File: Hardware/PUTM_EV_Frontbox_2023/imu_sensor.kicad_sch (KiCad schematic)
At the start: 3 parts, among them J2 Conn_01x05, J3 Conn_01x05, U17 IMS330DHCX

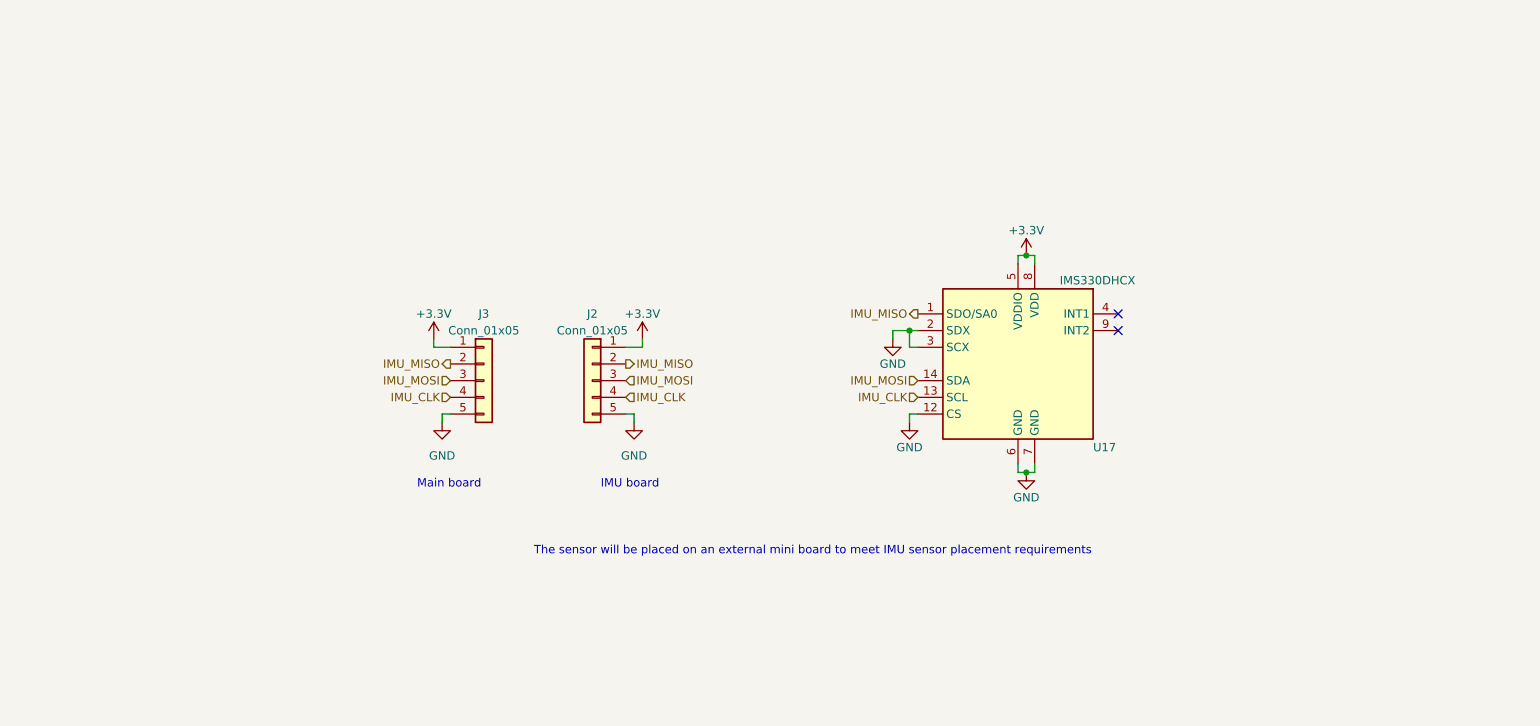
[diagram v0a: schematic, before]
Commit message: Added power section, replaced SWPS
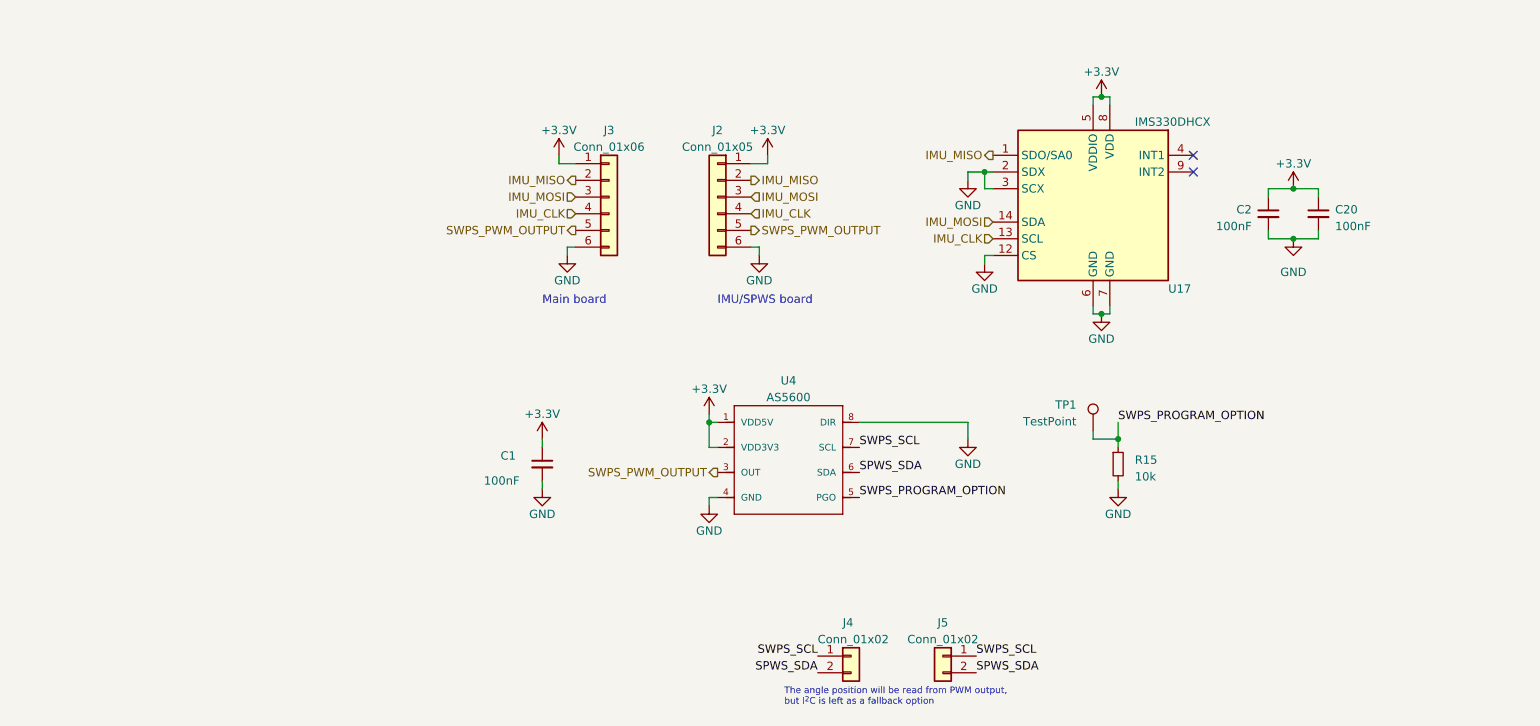
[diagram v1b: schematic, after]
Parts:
- added C1, C2, C20: 100nF, symbol Device:C_Small
- added J4, J5: Conn_01x02, symbol Connector_Generic:Conn_01x02
- added R15: 10k, symbol Device:R_Small
- added TP1: TestPoint, symbol Connector:TestPoint
- added U4: AS5600, AS5600, symbol AS5600:AS5600
- J2: symbol Connector_Generic:Conn_01x05 -> Connector_Generic:Conn_01x06
- J3: value Conn_01x05 -> Conn_01x06; symbol Connector_Generic:Conn_01x05 -> Connector_Generic:Conn_01x06
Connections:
- net +3.3V: now also C1.1, C2.1, C20.1, U4.1 (VDD5V), U4.2 (VDD3V3)
- net GND: now also J2.6 (Pin_6), J3.6 (Pin_6), C1.2, C2.2, C20.2, R15.2, U4.4 (GND), U4.8 (DIR); no longer J2.5 (Pin_5), J3.5 (Pin_5)
- new net SPWS_SDA: J4.2 (Pin_2), J5.2 (Pin_2), U4.6 (SDA)
- new net SWPS_PROGRAM_OPTION: R15.1, TP1.1, U4.5 (PGO)
- new net SWPS_PWM_OUTPUT: J2.5 (Pin_5), J3.5 (Pin_5), U4.3 (OUT)
- new net SWPS_SCL: J4.1 (Pin_1), J5.1 (Pin_1), U4.7 (SCL)
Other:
- note added: "IMU/SPWS board"
- note added: "The angle position will be read from PWM output, but I^{2}C is left as a fallback option"
- note removed: "IMU board"
- note removed: "The sensor will be placed on an external mini board to meet IMU sensor placement requirements"
- title: ISM330DHCX Sensor -> ISM330DHCX Sensor/Steering wheel position sensor
- moved on the sheet: U17

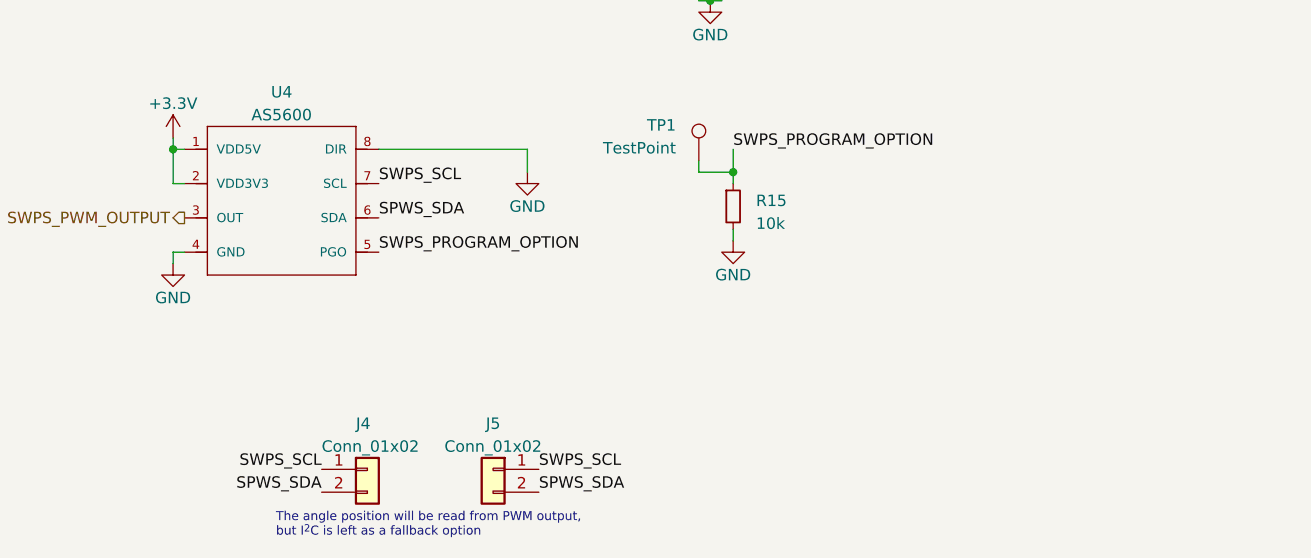
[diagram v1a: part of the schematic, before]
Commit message: Added MCU wiring
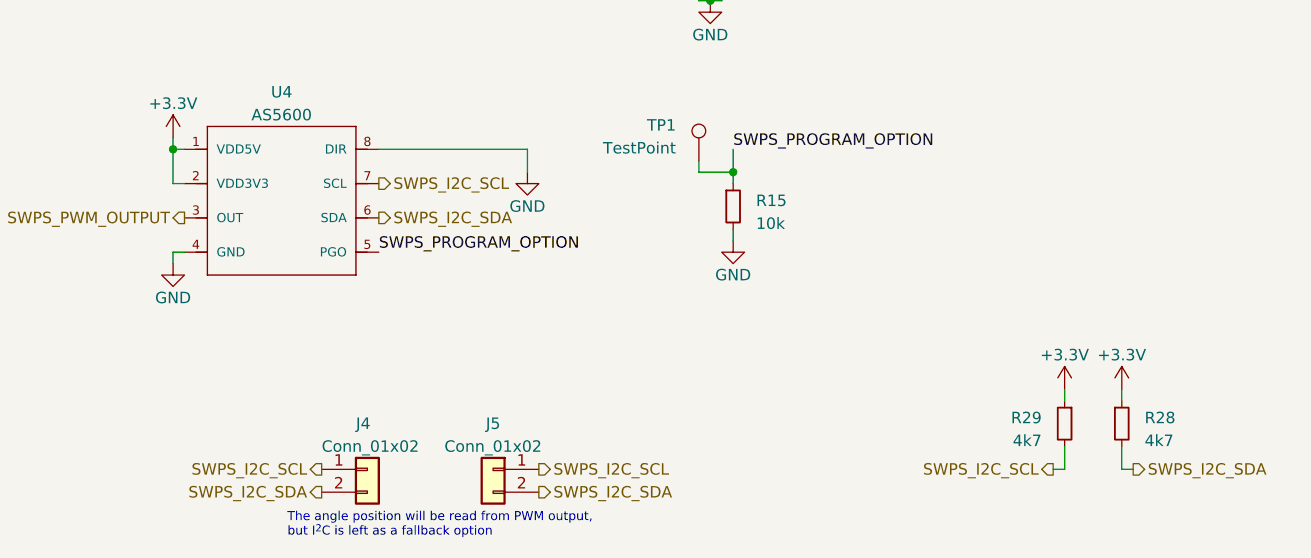
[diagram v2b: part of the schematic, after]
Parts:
- added R28, R29: 4k7, symbol Device:R_Small
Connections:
- net +3.3V: now also R28.1, R29.1
- net SPWS_SDA renamed SWPS_I2C_SDA
- net SWPS_I2C_SDA: now also R28.2
- net SWPS_SCL renamed SWPS_I2C_SCL
- net SWPS_I2C_SCL: now also R29.2
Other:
- title: ISM330DHCX Sensor/Steering wheel position sensor -> IMU and SWPS sensor
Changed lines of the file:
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@@
   (paper "A4")
   (title_block
-    (title "ISM330DHCX Sensor/Steering wheel position sensor")
+    (title "IMU and SWPS sensor")
     (date "2023-02-24")
     (rev "${REVISION}")
@@
     (stroke (width 0) (type default))
   )
+  (wire (pts (xy 228.6 147.32) (xy 228.6 144.78))
+    (stroke (width 0) (type default))
+  )
   (wire (pts (xy 129.54 72.39) (xy 132.08 72.39))
     (stroke (width 0) (type default))
   )
+  (wire (pts (xy 228.6 138.43) (xy 228.6 139.7))
+    (stroke (width 0) (type default))
+  )
   (wire (pts (xy 166.37 73.66) (xy 165.1 73.66))
     (stroke (width 0) (type default))
@@
     (stroke (width 0) (type default))
   )
+  (wire (pts (xy 222.25 138.43) (xy 222.25 139.7))
+    (stroke (width 0) (type default))
+  )
   (wire (pts (xy 181.61 95.25) (xy 182.88 95.25))
     (stroke (width 0) (type default))
@@
     (stroke (width 0) (type default))
   )
+  (wire (pts (xy 229.87 147.32) (xy 228.6 147.32))
+    (stroke (width 0) (type default))
+  )
   (wire (pts (xy 181.61 113.03) (xy 181.61 114.3))
     (stroke (width 0) (type default))
   )
+  (wire (pts (xy 220.98 147.32) (xy 222.25 147.32))
+    (stroke (width 0) (type default))
+  )
   (wire (pts (xy 165.1 86.36) (xy 166.37 86.36))
     (stroke (width 0) (type default))
@@
     (stroke (width 0) (type default))
   )
+  (wire (pts (xy 222.25 147.32) (xy 222.25 144.78))
+    (stroke (width 0) (type default))
+  )
   (wire (pts (xy 208.28 83.82) (xy 212.09 83.82))
     (stroke (width 0) (type default))
@@
   )
   (text "The angle position will be read from PWM output,\nbut I^{2}C is left as a fallback option"
-    (at 134.62 154.94 0)
+    (at 135.89 154.94 0)
     (effects (font (size 1 1)) (justify left bottom))
   )
@@
     (effects (font (size 1.27 1.27)) (justify left bottom))
   )
-  (label "SPWS_SDA" (at 139.7 149.86 180) (fields_autoplaced)
-    (effects (font (size 1.27 1.27)) (justify right bottom))
-  )
-  (label "SWPS_SCL" (at 163.83 147.32 0) (fields_autoplaced)
-    (effects (font (size 1.27 1.27)) (justify left bottom))
-  )
-  (label "SWPS_SCL" (at 139.7 147.32 180) (fields_autoplaced)
-    (effects (font (size 1.27 1.27)) (justify right bottom))
-  )
   (label "SWPS_PROGRAM_OPTION" (at 185.42 111.76 0) (fields_autoplaced)
     (effects (font (size 1.27 1.27)) (justify left bottom))
   )
-  (label "SPWS_SDA" (at 163.83 149.86 0) (fields_autoplaced)
-    (effects (font (size 1.27 1.27)) (justify left bottom))
-  )
-  (label "SPWS_SDA" (at 146.05 119.38 0) (fields_autoplaced)
-    (effects (font (size 1.27 1.27)) (justify left bottom))
-  )
   (label "SWPS_PROGRAM_OPTION" (at 146.05 123.19 0) (fields_autoplaced)
     (effects (font (size 1.27 1.27)) (justify left bottom))
   )
-  (label "SWPS_SCL" (at 146.05 115.57 0) (fields_autoplaced)
-    (effects (font (size 1.27 1.27)) (justify left bottom))
-  )
   (hierarchical_label "IMU_MOSI" (shape input) (at 129.54 77.47 0) (fields_autoplaced)
     (effects (font (size 1.27 1.27)) (justify left))
@@
     (effects (font (size 1.27 1.27)) (justify right))
   )
+  (hierarchical_label "SWPS_I2C_SDA" (shape output) (at 163.83 149.86 0) (fields_autoplaced)
+    (effects (font (size 1.27 1.27)) (justify left))
+  )
   (hierarchical_label "IMU_CLK" (shape input) (at 102.87 80.01 180) (fields_autoplaced)
     (effects (font (size 1.27 1.27)) (justify right))
@@
     (effects (font (size 1.27 1.27)) (justify right))
   )
+  (hierarchical_label "SWPS_I2C_SCL" (shape output) (at 146.05 115.57 0) (fields_autoplaced)
+    (effects (font (size 1.27 1.27)) (justify left))
+  )
+  (hierarchical_label "SWPS_I2C_SDA" (shape output) (at 146.05 119.38 0) (fields_autoplaced)
+    (effects (font (size 1.27 1.27)) (justify left))
+  )
+  (hierarchical_label "SWPS_I2C_SDA" (shape output) (at 139.7 149.86 180) (fields_autoplaced)
+    (effects (font (size 1.27 1.27)) (justify right))
+  )
   (hierarchical_label "SWPS_PWM_OUTPUT" (shape output) (at 102.87 82.55 180) (fields_autoplaced)
     (effects (font (size 1.27 1.27)) (justify right))
+  )
+  (hierarchical_label "SWPS_I2C_SCL" (shape output) (at 163.83 147.32 0) (fields_autoplaced)
+    (effects (font (size 1.27 1.27)) (justify left))
   )
   (hierarchical_label "SWPS_PWM_OUTPUT" (shape output) (at 129.54 82.55 0) (fields_autoplaced)
     (effects (font (size 1.27 1.27)) (justify left))
   )
+  (hierarchical_label "SWPS_I2C_SCL" (shape output) (at 220.98 147.32 180) (fields_autoplaced)
+    (effects (font (size 1.27 1.27)) (justify right))
+  )
   (hierarchical_label "IMU_MISO" (shape output) (at 129.54 74.93 0) (fields_autoplaced)
     (effects (font (size 1.27 1.27)) (justify left))
   )
+  (hierarchical_label "SWPS_I2C_SCL" (shape output) (at 139.7 147.32 180) (fields_autoplaced)
+    (effects (font (size 1.27 1.27)) (justify right))
+  )
   (hierarchical_label "IMU_MOSI" (shape input) (at 166.37 81.28 180) (fields_autoplaced)
     (effects (font (size 1.27 1.27)) (justify right))
   )
   (hierarchical_label "IMU_CLK" (shape input) (at 129.54 80.01 0) (fields_autoplaced)
+    (effects (font (size 1.27 1.27)) (justify left))
+  )
+  (hierarchical_label "SWPS_I2C_SDA" (shape output) (at 229.87 147.32 0) (fields_autoplaced)
     (effects (font (size 1.27 1.27)) (justify left))
   )
@@
         (path "/b652b05a-4e3d-4ad1-b032-18886abe7d45/fc1ffdcd-7b51-43f2-87c4-9a5d8609cd78"
           (reference "J3") (unit 1)
+        )
+      )
+    )
+  )
+  (symbol (lib_id "power:+3.3V") (at 228.6 138.43 0) (unit 1)
+    (in_bom yes) (on_board yes) (dnp no) (fields_autoplaced)
+    (property "Reference" "#PWR090" (at 228.6 142.24 0)
+      (effects (font (size 1.27 1.27)) hide)
+    )
+    (property "Value" "+3.3V" (at 228.6 134.62 0)
+      (effects (font (size 1.27 1.27)))
+    )
+    (property "Footprint" "" (at 228.6 138.43 0)
+      (effects (font (size 1.27 1.27)) hide)
+    )
+    (property "Datasheet" "" (at 228.6 138.43 0)
+      (effects (font (size 1.27 1.27)) hide)
+    )
+    (pin "1")
+    (instances
+      (project "PUTM_EV_Frontbox_2023"
+        (path "/b652b05a-4e3d-4ad1-b032-18886abe7d45/fc1ffdcd-7b51-43f2-87c4-9a5d8609cd78"
+          (reference "#PWR090") (unit 1)
         )
       )
@@
     )
   )
+  (symbol (lib_id "power:+3.3V") (at 222.25 138.43 0) (unit 1)
+    (in_bom yes) (on_board yes) (dnp no) (fields_autoplaced)
+    (property "Reference" "#PWR089" (at 222.25 142.24 0)
+      (effects (font (size 1.27 1.27)) hide)
+    )
+    (property "Value" "+3.3V" (at 222.25 134.62 0)
+      (effects (font (size 1.27 1.27)))
+    )
+    (property "Footprint" "" (at 222.25 138.43 0)
+      (effects (font (size 1.27 1.27)) hide)
+    )
+    (property "Datasheet" "" (at 222.25 138.43 0)
+      (effects (font (size 1.27 1.27)) hide)
+    )
+    (pin "1")
+    (instances
+      (project "PUTM_EV_Frontbox_2023"
+        (path "/b652b05a-4e3d-4ad1-b032-18886abe7d45/fc1ffdcd-7b51-43f2-87c4-9a5d8609cd78"
+          (reference "#PWR089") (unit 1)
+        )
+      )
+    )
+  )
   (symbol (lib_id "power:GND") (at 212.09 83.82 0) (unit 1)
     (in_bom yes) (on_board yes) (dnp no) (fields_autoplaced)
@@
         (path "/b652b05a-4e3d-4ad1-b032-18886abe7d45/fc1ffdcd-7b51-43f2-87c4-9a5d8609cd78"
           (reference "#PWR016") (unit 1)
+        )
+      )
+    )
+  )
+  (symbol (lib_id "Device:R_Small") (at 222.25 142.24 0) (mirror y) (unit 1)
+    (in_bom yes) (on_board yes) (dnp no)
+    (property "Reference" "R29" (at 219.71 141.605 0)
+      (effects (font (size 1.27 1.27)) (justify left))
+    )
+    (property "Value" "4k7" (at 219.71 144.145 0)
+      (effects (font (size 1.27 1.27)) (justify left))
+    )
+    (property "Footprint" "" (at 222.25 142.24 0)
+      (effects (font (size 1.27 1.27)) hide)
+    )
+    (property "Datasheet" "~" (at 222.25 142.24 0)
+      (effects (font (size 1.27 1.27)) hide)
+    )
+    (pin "1")
+    (pin "2")
+    (instances
+      (project "PUTM_EV_Frontbox_2023"
+        (path "/b652b05a-4e3d-4ad1-b032-18886abe7d45/fc1ffdcd-7b51-43f2-87c4-9a5d8609cd78"
+          (reference "R29") (unit 1)
         )
       )
@@
         )
       )
+    )
+  )
+  (symbol (lib_id "Device:R_Small") (at 228.6 142.24 0) (unit 1)
+    (in_bom yes) (on_board yes) (dnp no) (fields_autoplaced)
+    (property "Reference" "R28" (at 231.14 141.605 0)
+      (effects (font (size 1.27 1.27)) (justify left))
+    )
+    (property "Value" "4k7" (at 231.14 144.145 0)
+      (effects (font (size 1.27 1.27)) (justify left))
+    )
+    (property "Footprint" "" (at 228.6 142.24 0)
+      (effects (font (size 1.27 1.27)) hide)
+    )
+    (property "Datasheet" "~" (at 228.6 142.24 0)
+      (effects (font (size 1.27 1.27)) hide)
+    )
+    (pin "1")
+    (pin "2")
+    (instances
+      (project "PUTM_EV_Frontbox_2023"
+        (path "/b652b05a-4e3d-4ad1-b032-18886abe7d45/fc1ffdcd-7b51-43f2-87c4-9a5d8609cd78"
+          (reference "R28") (unit 1)
+        )
+      )

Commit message: Schematic ready for review
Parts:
- U17: symbol karta_pomiarowa_v2-rescue:LSM6DS3-Sensor_Motionn -> ISM330DHCX:LSM6DS3
- renumbered C1 to C2, C2 to C3, C20 to C4, J3 to J5, J2 to J6, J4 to J7, J5 to J8, R15 to R6, R29 to R7, R28 to R8, U4 to U2

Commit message: Fixed all issues
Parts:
- added C42: 1nF, symbol Device:C_Small
- added FB6, FB7: 60R@100MHz, symbol Device:FerriteBead_Small
- added R78: 1k, symbol Device:R_Small
- added TP10, TP7, TP8, TP9: TestPoint, symbol Connector:TestPoint
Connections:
- net +3.3V: now also FB6.1, FB7.1; no longer U17.5 (VDDIO), U17.8 (VDD), U2.1 (VDD5V), U2.2 (VDD3V3)
- net GND: now also C42.2
- net IMU_CLK: now also TP9.1
- net IMU_MISO: now also TP7.1
- net IMU_MOSI: now also TP8.1
- net SWPS_PWM_OUTPUT: now also C42.1, R78.2; no longer U2.3 (OUT)
- new net: FB7.2, U2.1 (VDD5V), U2.2 (VDD3V3)
- new net: FB6.2, U17.5 (VDDIO), U17.8 (VDD)
- new net SWPS_RAW_PWM_OUTPUT: R78.1, TP10.1, U2.3 (OUT)
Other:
- note added: "IC is used in mode 1 >>>"
- note added: "IMU/SWPS board"
- note added: "The min unfiltered rise time is 1.8 us"
- note removed: "IMU/SPWS board"
- moved on the sheet: C2
